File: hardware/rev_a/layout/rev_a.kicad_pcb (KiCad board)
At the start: 4 copper layers, 78 x 58 mm, 68 parts, among them J1 HTSW-110-07-T-D, J2 HTSW-110-07-T-D, U1 ADS1299-4PAGR, U2 TPS7A2033PDBVR

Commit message: feat(hardware): reconstruct routed C4 service access and carrier backing
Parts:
- added J3: B6B-XH-A(LF)(SN), Connector_JST:JST_XH_B6B-XH-A_1x06_P2.50mm_Vertical, F.Cu at (75.0, 15.0)
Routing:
- net AVDD: track 241.2 -> 261.1 mm
- net DVDD: track 49.7 -> 68.0 mm

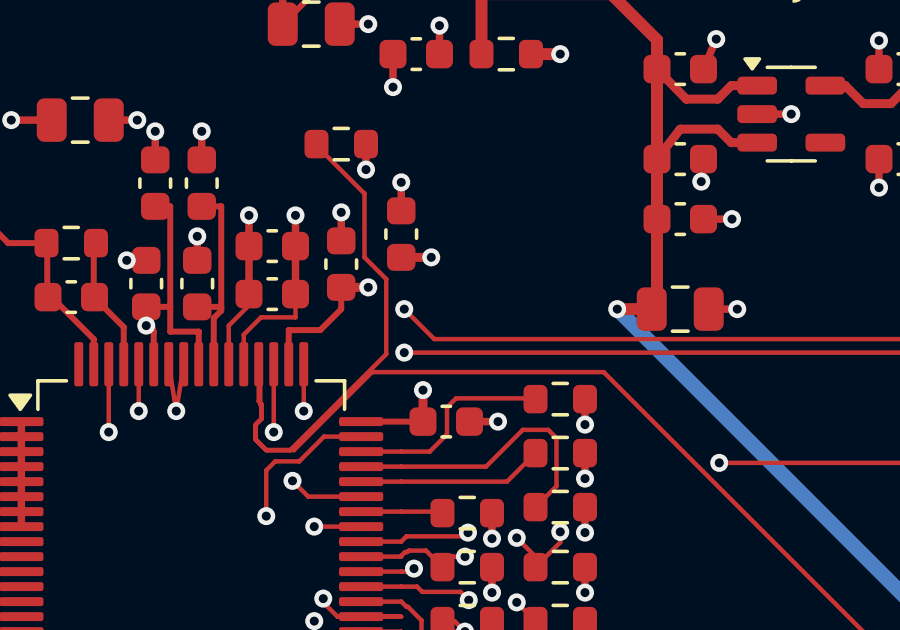
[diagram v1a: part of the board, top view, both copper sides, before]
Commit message: feat(hardware): apply the preserved five-position SPI source candidate
Apply exactly eleven manifest-verified files on 08a8ddd0, retaining
all later DNP, preservation, selection and native-fault test repairs.
The historical patch reproduces 2e50d2b; no geometry is recreated.
Five positions remain DNP/NOT_SELECTED. Native exports and copper
fills are not refreshed here. This is source publication only, not
a passing gate, approved damping value or fabrication release.
No workflow, firmware, Q1, dependency or permission setting changes
are included in this engineering commit. No project code executed
by the isolated source publisher. PR98 must remain draft.
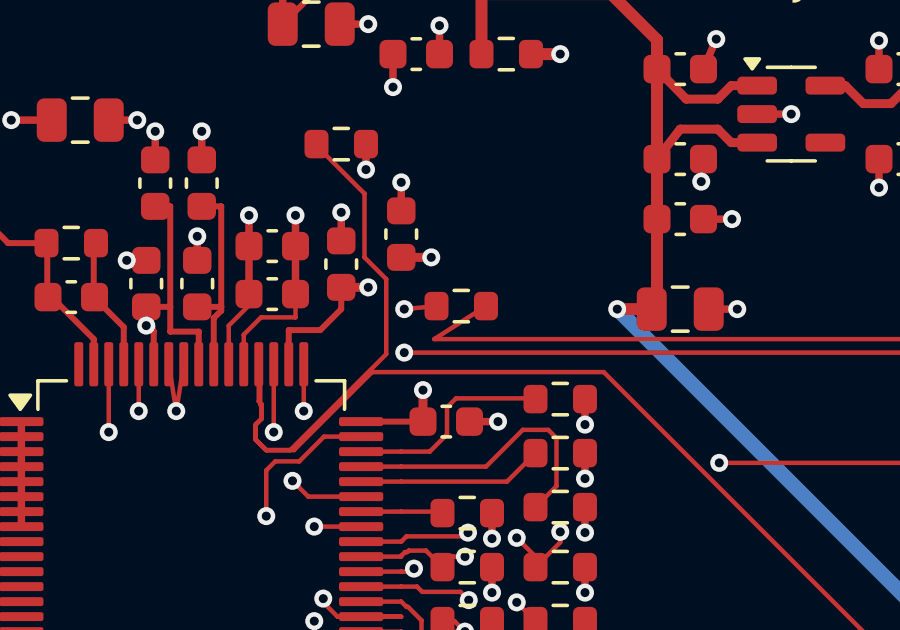
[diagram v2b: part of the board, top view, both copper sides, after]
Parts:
- added R24: NOT_SELECTED, Resistor_SMD:R_0603_1608Metric, F.Cu at (57.0, 29.4)
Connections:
- U1 pad 43: MISO -> MISO_DRV
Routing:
- net MISO_DRV: track 0.00 -> 10.9 mm, vias 0 -> 2
- net MISO: track 35.7 -> 26.6 mm, vias 2 -> 0
